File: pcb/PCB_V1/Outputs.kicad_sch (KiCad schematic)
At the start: 21 parts, among them J501 FAN1 / 3.5 mm, J511 FAN2 / 3.5 mm, J521 PUMP 24V / 6W, Q501 AO3400A, Q511 AO3400A, Q521 AO3422

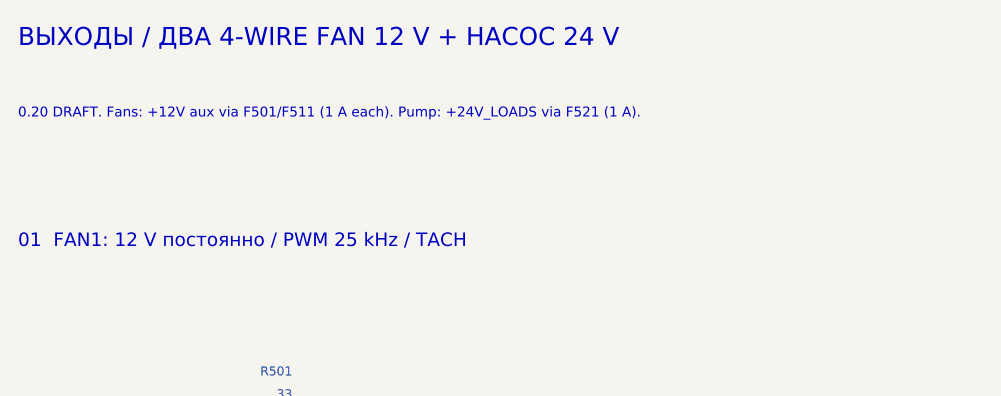
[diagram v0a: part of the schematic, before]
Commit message: pcb: use low-leakage RTC supply diode for revision 0.21
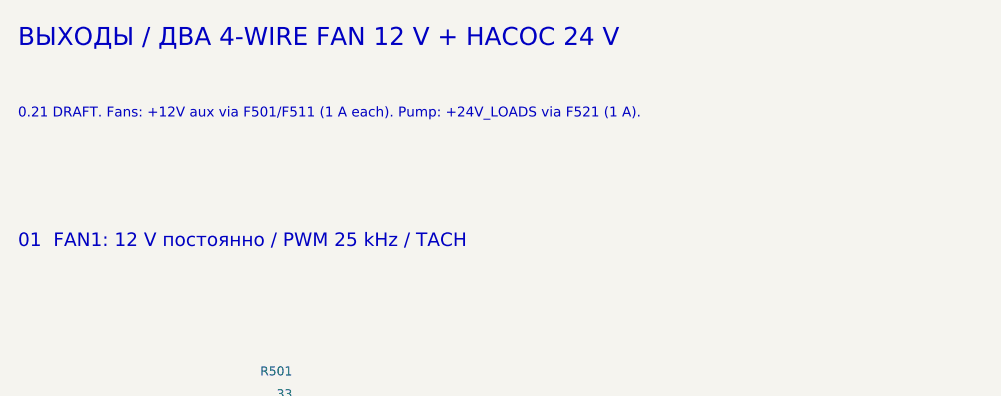
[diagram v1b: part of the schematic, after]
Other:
- note added: "0.21 DRAFT. Fans: +12V aux via F501/F511 (1 A each). Pump: +24V_LOADS via F521 (1 A)."
- note removed: "0.20 DRAFT. Fans: +12V aux via F501/F511 (1 A each). Pump: +24V_LOADS via F521 (1 A)."
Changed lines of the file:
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@@
 	(title_block
 		(title "04 - Fans (12 V aux) and pump (24 V)")
-		(date "2026-09-29")
-		(rev "0.20-DRAFT")
+		(date "2026-09-30")
+		(rev "0.21-DRAFT")
 		(company "GrowBox controller")
 		(comment 1 "Simplified prototype; unrouted; hardware qualification pending")
@@
 		)
 	)
-	(text "0.20 DRAFT. Fans: +12V aux via F501/F511 (1 A each). Pump: +24V_LOADS via F521 (1 A)."
+	(text "0.21 DRAFT. Fans: +12V aux via F501/F511 (1 A each). Pump: +24V_LOADS via F521 (1 A)."
 		(exclude_from_sim no)
 		(at 20.32 24.13 0)
